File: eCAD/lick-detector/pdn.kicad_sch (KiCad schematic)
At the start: 16 parts, among them J2 J_PinHeader_01x02_2.54_V, J3 J_PinHeader_01x02_2.54_V, U1 LM27762DSSR

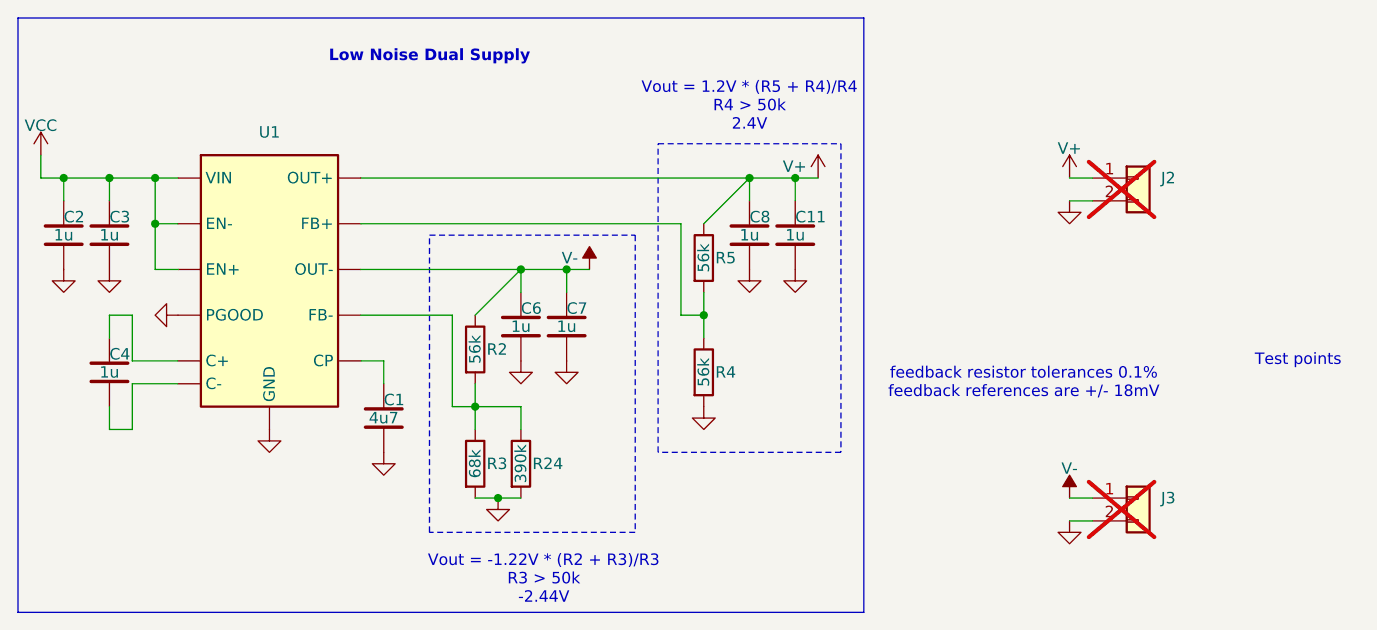
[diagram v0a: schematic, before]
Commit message: Number of upgrades complete: - Lower amplitude sine wave generator - Improved debug connector layout - Brightness of LED decreased - README updated with guide and areas for documentation - .gitignore added to ignore backup files and temporary files
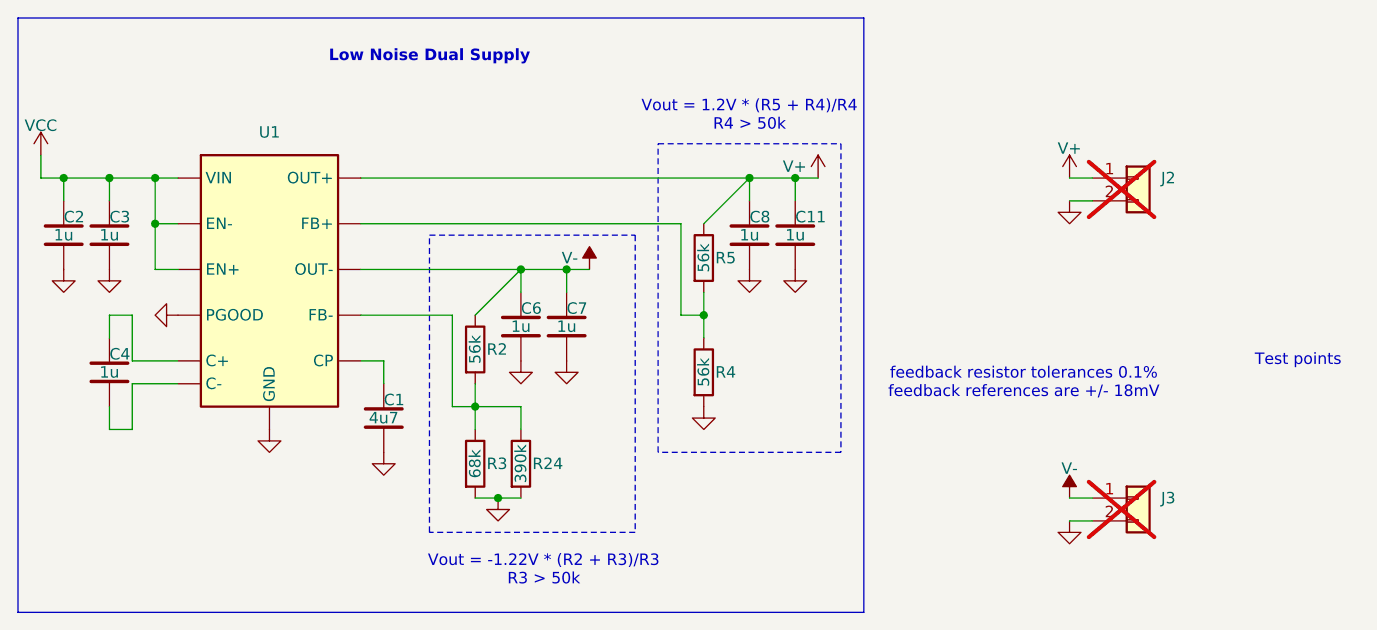
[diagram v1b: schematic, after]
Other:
- note added: "Vout = -1.22V * (R2 + R3)/R3 R3 > 50k"
- note added: "Vout = 1.2V * (R5 + R4)/R4 R4 > 50k"
- note removed: "Vout = -1.22V * (R2 + R3)/R3 R3 > 50k -2.44V"
- note removed: "Vout = 1.2V * (R5 + R4)/R4 R4 > 50k 2.4V"
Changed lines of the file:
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@@
 		)
 	)
-	(text "Vout = 1.2V * (R5 + R4)/R4\nR4 > 50k\n2.4V"
+	(text "Vout = 1.2V * (R5 + R4)/R4\nR4 > 50k"
 		(exclude_from_sim no)
 		(at 190.5 68.58 0)
@@
 		)
 	)
-	(text "Vout = -1.22V * (R2 + R3)/R3\nR3 > 50k\n-2.44V"
+	(text "Vout = -1.22V * (R2 + R3)/R3\nR3 > 50k\n"
 		(exclude_from_sim no)
 		(at 167.64 115.57 0)
